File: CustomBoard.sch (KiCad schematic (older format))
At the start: 37 parts, among them J1 RIGHT, J10 Sensor08, J11 Sensor09, J12 Sensor10, J13 Sensor11, J14 Sensor12, J2 LEFT, J3 Sensor01, J4 Sensor02, J5 Sensor03, J6 Sensor04, J7 Sensor05, J8 Sensor06, J9 Sensor07, U1 DS28E05, U2 PCA9555, U3 VL53L1X

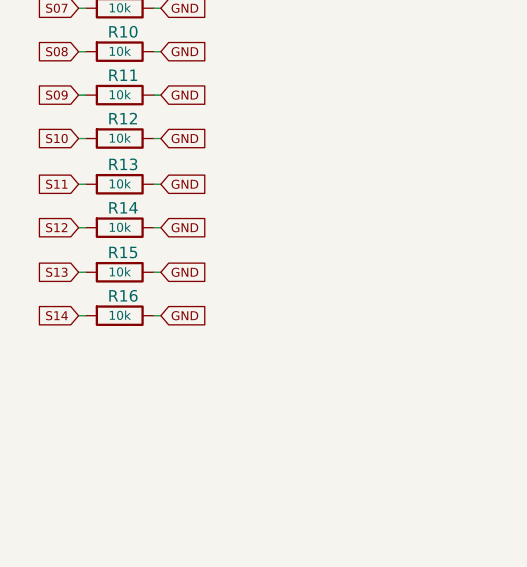
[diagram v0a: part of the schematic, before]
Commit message: pads missing
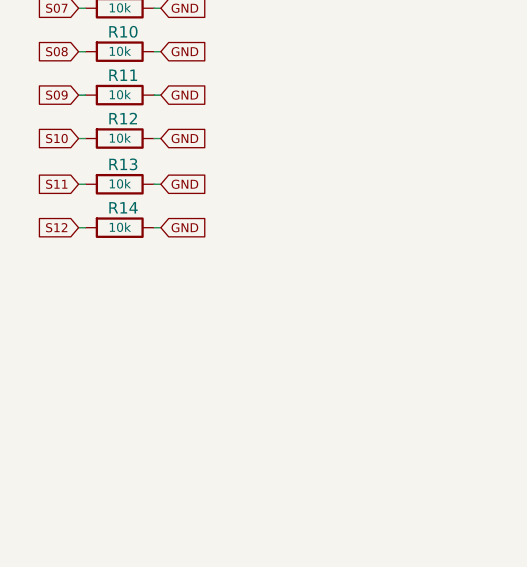
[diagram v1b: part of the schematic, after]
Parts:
- removed R15, R16: 10k, Resistors_SMD:R_0402, symbol R
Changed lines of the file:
@@
 Wire Wire Line
 	1100 3325 1130 3325
-Text GLabel 770  3520 0    39   Input ~ 0
-S13
-Text GLabel 1130 3520 2    39   Input ~ 0
-GND
-$Comp
-L R R15
-U 1 1 5B5F744E
-P 950 3520
-F 0 "R15" V 865 3535 50  0000 C CNN
-F 1 "10k" V 950 3520 39  0000 C CNN
-F 2 "Resistors_SMD:R_0402" V 880 3520 50  0001 C CNN
-F 3 "" H 950 3520 50  0001 C CNN
-	1    950  3520
-	0    1    1    0
-$EndComp
-Wire Wire Line
-	800  3520 770  3520
-Wire Wire Line
-	1100 3520 1130 3520
-Text GLabel 770  3710 0    39   Input ~ 0
-S14
-Text GLabel 1130 3710 2    39   Input ~ 0
-GND
-$Comp
-L R R16
-U 1 1 5B5F7458
-P 950 3710
-F 0 "R16" V 865 3725 50  0000 C CNN
-F 1 "10k" V 950 3710 39  0000 C CNN
-F 2 "Resistors_SMD:R_0402" V 880 3710 50  0001 C CNN
-F 3 "" H 950 3710 50  0001 C CNN
-	1    950  3710
-	0    1    1    0
-$EndComp
-Wire Wire Line
-	800  3710 770  3710
-Wire Wire Line
-	1100 3710 1130 3710
 NoConn ~ 6600 4410
 NoConn ~ 6600 4265

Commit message: complete board
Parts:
- J1: footprint Pin_Headers:Pin_Header_Straight_1x10_Pitch2.00mm_SMD_Pin1Right -> footprint:BF090-10-X-B2
- J2: footprint Pin_Headers:Pin_Header_Straight_1x10_Pitch2.00mm_SMD_Pin1Left -> footprint:BF090-10-X-B2
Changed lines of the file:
@@
 F 0 "J1" H 910 7610 50  0000 C CNN
 F 1 "RIGHT" H 910 6510 50  0000 C CNN
-F 2 "Pin_Headers:Pin_Header_Straight_1x10_Pitch2.00mm_SMD_Pin1Right" H 910 7110 50  0001 C CNN
+F 2 "footprint:BF090-10-X-B2" H 910 7110 50  0001 C CNN
 F 3 "" H 910 7110 50  0001 C CNN
 	1    910  7110
@@
 F 0 "J2" H 1730 7610 50  0000 C CNN
 F 1 "LEFT" H 1730 6510 50  0000 C CNN
-F 2 "Pin_Headers:Pin_Header_Straight_1x10_Pitch2.00mm_SMD_Pin1Left" H 1730 7110 50  0001 C CNN
+F 2 "footprint:BF090-10-X-B2" H 1730 7110 50  0001 C CNN
 F 3 "" H 1730 7110 50  0001 C CNN
 	1    1730 7110

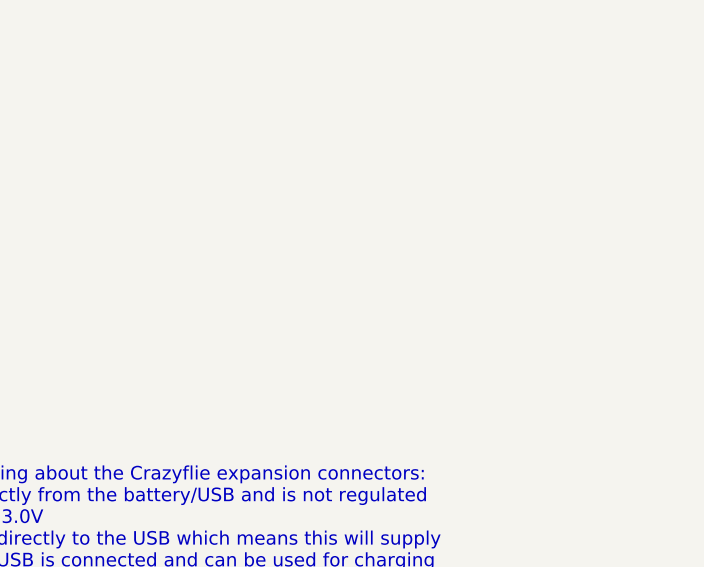
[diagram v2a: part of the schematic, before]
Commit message: integrate cam module in main board
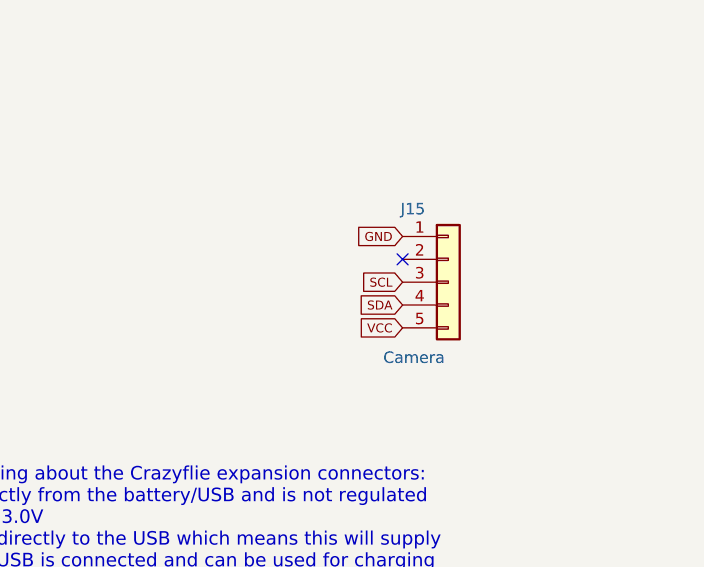
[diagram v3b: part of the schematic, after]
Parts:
- added J15: Camera, footprint:AMGCam, symbol Conn_01x05
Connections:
- net GND: now also J15.1 (Pin_1)
- net SCL: now also J15.3 (Pin_3)
- net SDA: now also J15.4 (Pin_4)
- net VCC: now also J15.5 (Pin_5)
- no-connect marks 22 -> 23
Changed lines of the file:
@@
 Wire Notes Line
 	7155 510  11180 510
+$Comp
+L Conn_01x05 J15
+U 1 1 5B6259FC
+P 10780 5760
+F 0 "J15" H 10625 6080 50  0000 C CNN
+F 1 "Camera" H 10630 5430 50  0000 C CNN
+F 2 "footprint:AMGCam" H 10780 5760 50  0001 C CNN
+F 3 "" H 10780 5760 50  0001 C CNN
+	1    10780 5760
+	1    0    0    -1
+$EndComp
+Text GLabel 10580 5560 0    39   Input ~ 0
+GND
+Text GLabel 10580 5760 0    39   Input ~ 0
+SCL
+Text GLabel 10580 5860 0    39   Input ~ 0
+SDA
+Text GLabel 10580 5960 0    39   Input ~ 0
+VCC
+NoConn ~ 10580 5660
 $EndSCHEMATC

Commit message: reformatting
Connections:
- no-connect marks 23 -> 22
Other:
- note added: "Camera Slot"
- note added: "ToF Pullups"
- moved on the sheet: D1, J15, R1, R10, R11, R12, R13, R14, R2, R3, R5, R6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

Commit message: ready
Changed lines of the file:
@@
 $Descr A4 11693 8268
 encoding utf-8
-Sheet 1 1
+Sheet 1 18
 Title "CrazyFlie2.0"
 Date "2018-07-24"
@@
 Text Notes 9905 2510 0    59   Italic 12
 ToF Pullups
+$Sheet
+S 8385 5485 1105 780
+U 5B640D2F
+F0 "ToFSensors" 39
+F1 "ToFSensors.sch" 39
+$EndSheet
+$Sheet
+S 7130 5485 1145 780
+U 5B640EC2
+F0 "Camera" 39
+F1 "Camera.sch" 39
+$EndSheet
 $EndSCHEMATC

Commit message: update
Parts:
- removed U2: PCA9555, Housings_DFN_QFN:QFN-24_4x4mm_Pitch0.5mm, symbol PCA9555
- added U2: PCA9555X, Housings_SSOP:TSSOP-24_4.4x7.8mm_Pitch0.65mm, symbol PCA9555X
- C1, C2, C3: footprint Capacitors_SMD:C_0402 -> Capacitors_SMD:C_0603
- D1: footprint LEDs:LED_0402 -> LEDs:LED_0603
- R1, R10, R11, R12, R13, R14, R2, R3, R4, R5, R6, R7, R8, R9: footprint Resistors_SMD:R_0402 -> Resistors_SMD:R_0603
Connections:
- net GND: now also U2.12 (GND), U2.2 (A1), U2.21 (A0), U2.3 (A2)
- net S01: now also J6.2 (Pin_2), R6.2, U2.5 (P01); no longer J3.2 (Pin_2), R2.2
- net S02: now also J7.2 (Pin_2), R7.2, U2.6 (P02); no longer J4.2 (Pin_2), R3.2
- net S03: now also J8.2 (Pin_2), R8.2, U2.7 (P03); no longer J5.2 (Pin_2), R5.2
- net S04: now also J9.2 (Pin_2), R9.2, U2.8 (P04); no longer J6.2 (Pin_2), R6.2
- net S05: now also J10.2 (Pin_2), R10.2, U2.9 (P05); no longer J7.2 (Pin_2), R7.2
- net S06: now also J11.2 (Pin_2), R11.2, U2.10 (P06); no longer J8.2 (Pin_2), R8.2
- net S07: now also J12.2 (Pin_2), R12.2, U2.11 (P07); no longer J9.2 (Pin_2), R9.2
- net S08: now also J13.2 (Pin_2), R13.2, U2.13 (P10); no longer J10.2 (Pin_2), R10.2
- net S09: now also J14.2 (Pin_2), R14.2, U2.14 (P11); no longer J11.2 (Pin_2), R11.2
- net S10: now also J3.2 (Pin_2), R2.2, U2.15 (P12); no longer J12.2 (Pin_2), R12.2
- net S11: now also J4.2 (Pin_2), R3.2, U2.16 (P13); no longer J13.2 (Pin_2), R13.2
- net S12: now also J5.2 (Pin_2), R5.2, U2.17 (P14); no longer J14.2 (Pin_2), R14.2
- net S15: now also U2.20 (P17)
- net SCL: now also U2.22 (SCL)
- net SDA: now also U2.23 (SDA)
- net VCC: now also U2.24 (VCC)
- net at D1.1 (K): now also U2.4 (P00)
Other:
- moved on the sheet: D1, R1
